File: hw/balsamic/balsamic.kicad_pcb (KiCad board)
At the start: 2 copper layers, 3 parts, among them U1 ISP1807-LR-RS, U2 BMI160, U3 K210

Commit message: Add hardware files
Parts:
- added J1: Conn_01x24, Connector_FFC-FPC:Hirose_FH12-24S-0.5SH_1x24-1MP_P0.50mm_Horizontal, F.Cu at (195.0, 35.1)
- added J2: USB_C_Receptacle_USB2.0, Connector_USB:USB_C_Receptacle_XKB_U262-16XN-4BVC11, F.Cu at (167.7, 38.7)
- added U4: CH552T, Package_SO:TSSOP-20_4.4x6.5mm_P0.65mm, F.Cu at (185.6, 31.8)
- added U5: GD25LQ, footprints:SOIC127P790X216-8N, F.Cu at (170.2, 25.7)
- moved U3 28.5 mm to (176.8, 39.9)
- moved U2 18.0 mm to (179.0, 33.9)
- moved U1 12.1 mm to (185.6, 39.9)

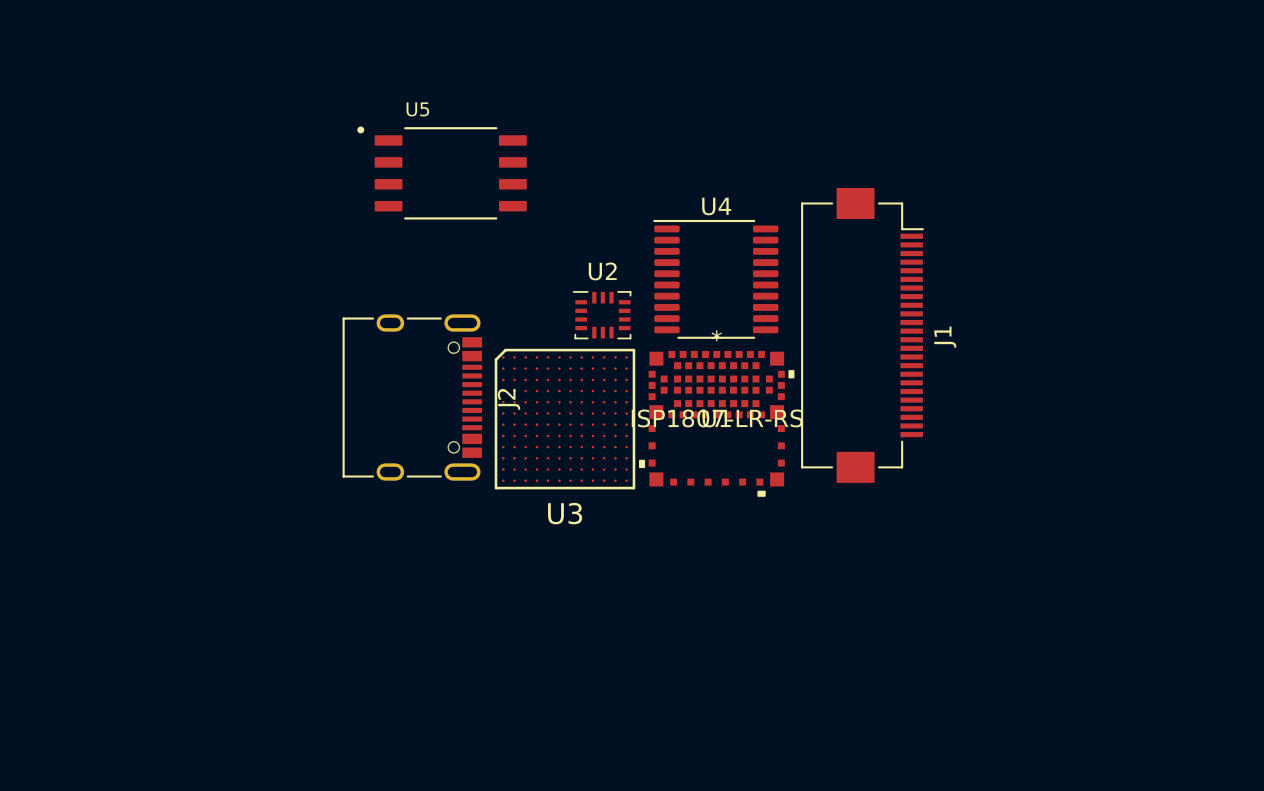
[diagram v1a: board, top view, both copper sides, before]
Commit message: PCB Schematic Layout
Finished schematic layout for MAX77658, power input to kendryte and some
of the signals for the kendryte IO.

I am beginning the layout for the ISP.
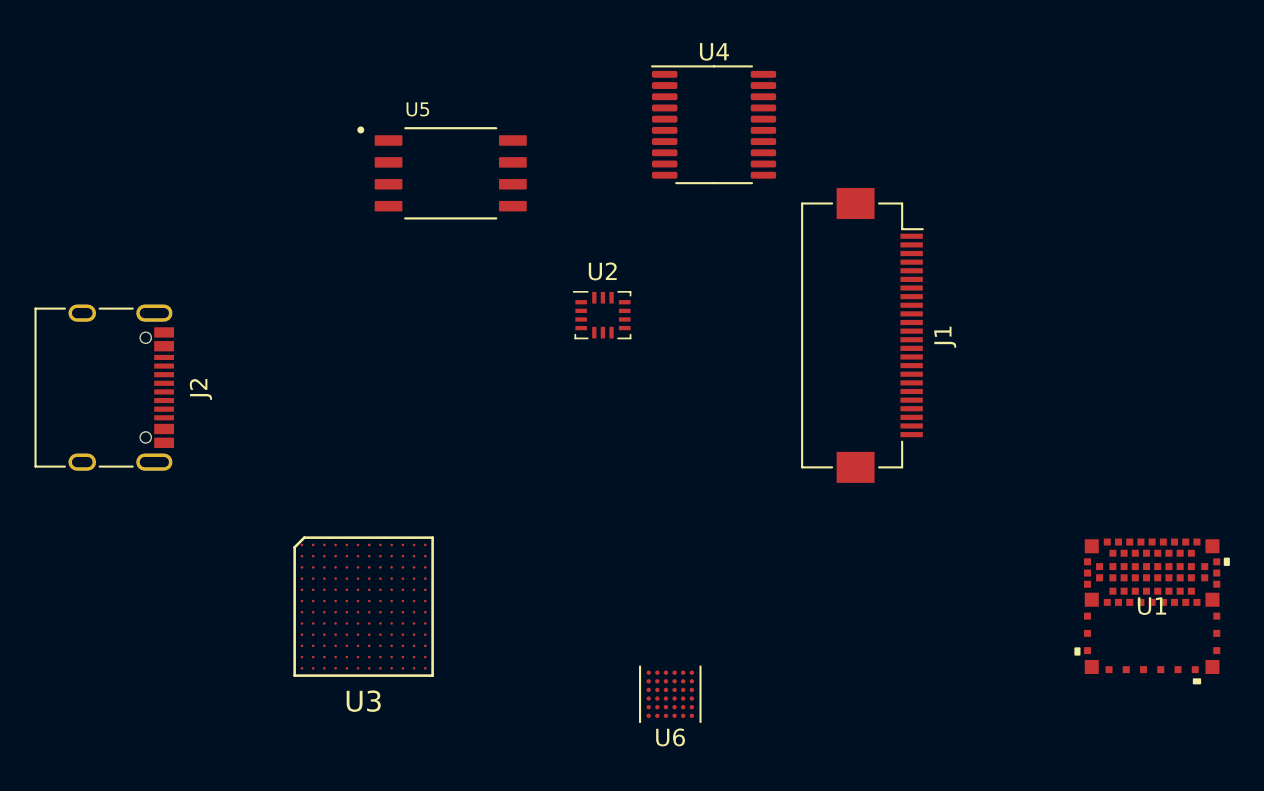
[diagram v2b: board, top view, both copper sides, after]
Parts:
- added U6: MAX77658AANX+, footprints:MAX77658AANX&plus_, F.Cu at (182.9, 55.9)
- moved U1 27.5 mm to (210.8, 50.8)
- moved J2 17.9 mm to (149.9, 38.1)
- moved U3 16.0 mm to (165.1, 50.8)
- moved U4 8.97 mm to (185.4, 22.9)
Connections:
- J1 pad 1: Net-(J1-Pad1) -> unconnected-(J1-Pad1)
- J1 pad 10: Net-(J1-Pad10) -> unconnected-(J1-Pad10)
- J1 pad 11: Net-(J1-Pad11) -> unconnected-(J1-Pad11)
- J1 pad 12: Net-(J1-Pad12) -> unconnected-(J1-Pad12)
- J1 pad 13: Net-(J1-Pad13) -> unconnected-(J1-Pad13)
- J1 pad 14: Net-(J1-Pad14) -> unconnected-(J1-Pad14)
- J1 pad 15: Net-(J1-Pad15) -> unconnected-(J1-Pad15)
- J1 pad 16: Net-(J1-Pad16) -> unconnected-(J1-Pad16)
- J1 pad 17: Net-(J1-Pad17) -> unconnected-(J1-Pad17)
- J1 pad 18: Net-(J1-Pad18) -> unconnected-(J1-Pad18)
- J1 pad 19: Net-(J1-Pad19) -> unconnected-(J1-Pad19)
- J1 pad 2: Net-(J1-Pad2) -> unconnected-(J1-Pad2)
- J1 pad 20: Net-(J1-Pad20) -> unconnected-(J1-Pad20)
- J1 pad 21: Net-(J1-Pad21) -> unconnected-(J1-Pad21)
- J1 pad 22: Net-(J1-Pad22) -> unconnected-(J1-Pad22)
- J1 pad 23: Net-(J1-Pad23) -> unconnected-(J1-Pad23)
- J1 pad 24: Net-(J1-Pad24) -> unconnected-(J1-Pad24)
- J1 pad 3: Net-(J1-Pad3) -> unconnected-(J1-Pad3)
- J1 pad 4: Net-(J1-Pad4) -> unconnected-(J1-Pad4)
- J1 pad 5: Net-(J1-Pad5) -> unconnected-(J1-Pad5)
- J1 pad 6: Net-(J1-Pad6) -> unconnected-(J1-Pad6)
- J1 pad 7: Net-(J1-Pad7) -> unconnected-(J1-Pad7)
- J1 pad 8: Net-(J1-Pad8) -> unconnected-(J1-Pad8)
- J1 pad 9: Net-(J1-Pad9) -> unconnected-(J1-Pad9)
- J2 pad A5: Net-(J2-PadA5) -> unconnected-(J2-PadA5)
- J2 pad A6: Net-(J2-PadA6) -> unconnected-(J2-PadA6)
- J2 pad A7: Net-(J2-PadA7) -> unconnected-(J2-PadA7)
- J2 pad A8: Net-(J2-PadA8) -> unconnected-(J2-PadA8)
- J2 pad B5: Net-(J2-PadB5) -> unconnected-(J2-PadB5)
- J2 pad B6: Net-(J2-PadB6) -> unconnected-(J2-PadB6)
- J2 pad B7: Net-(J2-PadB7) -> unconnected-(J2-PadB7)
- J2 pad B8: Net-(J2-PadB8) -> unconnected-(J2-PadB8)
- J2 pad S1: Net-(J2-PadS1) -> unconnected-(J2-PadS1)
- U1 pad 1: Net-(U1-Pad1) -> unconnected-(U1-Pad1)
- U1 pad 10: Net-(U1-Pad10) -> unconnected-(U1-Pad10)
- U1 pad 11: Net-(U1-Pad11) -> unconnected-(U1-Pad11)
- U1 pad 12: Net-(U1-Pad12) -> unconnected-(U1-Pad12)
- U1 pad 13: Net-(U1-Pad13) -> unconnected-(U1-Pad13)
- U1 pad 14: Net-(U1-Pad14) -> unconnected-(U1-Pad14)
- U1 pad 15: Net-(U1-Pad15) -> unconnected-(U1-Pad15)
- U1 pad 16: Net-(U1-Pad16) -> unconnected-(U1-Pad16)
- U1 pad 17: Net-(U1-Pad17) -> unconnected-(U1-Pad17)
- U1 pad 18: Net-(U1-Pad18) -> unconnected-(U1-Pad18)
- U1 pad 19: Net-(U1-Pad19) -> unconnected-(U1-Pad19)
- U1 pad 2: Net-(U1-Pad2) -> unconnected-(U1-Pad2)
- U1 pad 20: Net-(U1-Pad20) -> unconnected-(U1-Pad20)
- U1 pad 21: Net-(U1-Pad21) -> unconnected-(U1-Pad21)
- U1 pad 22: Net-(U1-Pad22) -> unconnected-(U1-Pad22)
- U1 pad 23: Net-(U1-Pad23) -> unconnected-(U1-Pad23)
- U1 pad 24: Net-(U1-Pad24) -> unconnected-(U1-Pad24)
- U1 pad 25: Net-(U1-Pad25) -> unconnected-(U1-Pad25)
- U1 pad 26: Net-(U1-Pad26) -> unconnected-(U1-Pad26)
- U1 pad 27: Net-(U1-Pad27) -> unconnected-(U1-Pad27)
- U1 pad 28: Net-(U1-Pad28) -> unconnected-(U1-Pad28)
- U1 pad 29: Net-(U1-Pad29) -> unconnected-(U1-Pad29)
- U1 pad 3: Net-(U1-Pad3) -> unconnected-(U1-Pad3)
- U1 pad 30: Net-(U1-Pad30) -> unconnected-(U1-Pad30)
- U1 pad 31: Net-(U1-Pad31) -> unconnected-(U1-Pad31)
- U1 pad 32: Net-(U1-Pad32) -> unconnected-(U1-Pad32)
- U1 pad 33: Net-(U1-Pad33) -> unconnected-(U1-Pad33)
- U1 pad 34: Net-(U1-Pad34) -> unconnected-(U1-Pad34)
- U1 pad 35: Net-(U1-Pad35) -> unconnected-(U1-Pad35)
- U1 pad 36: Net-(U1-Pad36) -> unconnected-(U1-Pad36)
- U1 pad 37: Net-(U1-Pad37) -> unconnected-(U1-Pad37)
- U1 pad 38: Net-(U1-Pad38) -> unconnected-(U1-Pad38)
- U1 pad 39: Net-(U1-Pad39) -> unconnected-(U1-Pad39)
- U1 pad 4: Net-(U1-Pad4) -> unconnected-(U1-Pad4)
- U1 pad 40: Net-(U1-Pad40) -> unconnected-(U1-Pad40)
- U1 pad 41: Net-(U1-Pad41) -> unconnected-(U1-Pad41)
- U1 pad 42: Net-(U1-Pad42) -> unconnected-(U1-Pad42)
- U1 pad 43: Net-(U1-Pad43) -> unconnected-(U1-Pad43)
- U1 pad 44: Net-(U1-Pad44) -> unconnected-(U1-Pad44)
- U1 pad 45: Net-(U1-Pad45) -> unconnected-(U1-Pad45)
- U1 pad 46: Net-(U1-Pad46) -> unconnected-(U1-Pad46)
- U1 pad 47: Net-(U1-Pad47) -> unconnected-(U1-Pad47)
- U1 pad 48: Net-(U1-Pad48) -> unconnected-(U1-Pad48)
- U1 pad 49: Net-(U1-Pad49) -> unconnected-(U1-Pad49)
- U1 pad 5: Net-(U1-Pad5) -> unconnected-(U1-Pad5)
- U1 pad 50: Net-(U1-Pad50) -> unconnected-(U1-Pad50)
- U1 pad 51: Net-(U1-Pad51) -> unconnected-(U1-Pad51)
- U1 pad 52: Net-(U1-Pad52) -> unconnected-(U1-Pad52)
- U1 pad 53: Net-(U1-Pad53) -> unconnected-(U1-Pad53)
- U1 pad 54: Net-(U1-Pad54) -> unconnected-(U1-Pad54)
- U1 pad 55: Net-(U1-Pad55) -> unconnected-(U1-Pad55)
- U1 pad 56: Net-(U1-Pad56) -> unconnected-(U1-Pad56)
- U1 pad 57: Net-(U1-Pad57) -> unconnected-(U1-Pad57)
- U1 pad 58: Net-(U1-Pad58) -> unconnected-(U1-Pad58)
- U1 pad 59: Net-(U1-Pad59) -> unconnected-(U1-Pad59)
- U1 pad 6: Net-(U1-Pad6) -> unconnected-(U1-Pad6)
- U1 pad 60: Net-(U1-Pad60) -> unconnected-(U1-Pad60)
- U1 pad 61: Net-(U1-Pad61) -> unconnected-(U1-Pad61)
- U1 pad 62: Net-(U1-Pad62) -> unconnected-(U1-Pad62)
- U1 pad 63: Net-(U1-Pad63) -> unconnected-(U1-Pad63)
- U1 pad 64: Net-(U1-Pad64) -> unconnected-(U1-Pad64)
- U1 pad 65: Net-(U1-Pad65) -> unconnected-(U1-Pad65)
- U1 pad 66: Net-(U1-Pad66) -> unconnected-(U1-Pad66)
- U1 pad 67: Net-(U1-Pad67) -> unconnected-(U1-Pad67)
- U1 pad 68: Net-(U1-Pad68) -> unconnected-(U1-Pad68)
- U1 pad 69: Net-(U1-Pad69) -> unconnected-(U1-Pad69)
- U1 pad 7: Net-(U1-Pad7) -> unconnected-(U1-Pad7)
- U1 pad 70: Net-(U1-Pad70) -> unconnected-(U1-Pad70)
- U1 pad 71: Net-(U1-Pad71) -> unconnected-(U1-Pad71)
- U1 pad 72: Net-(U1-Pad72) -> unconnected-(U1-Pad72)
- U1 pad 73: Net-(U1-Pad73) -> unconnected-(U1-Pad73)
- U1 pad 74: Net-(U1-Pad74) -> unconnected-(U1-Pad74)
- U1 pad 75: Net-(U1-Pad75) -> unconnected-(U1-Pad75)
- U1 pad 76: Net-(U1-Pad76) -> unconnected-(U1-Pad76)
- U1 pad 77: Net-(U1-Pad77) -> unconnected-(U1-Pad77)
- U1 pad 78: Net-(U1-Pad78) -> unconnected-(U1-Pad78)
- U1 pad 8: Net-(U1-Pad8) -> unconnected-(U1-Pad8)
- U1 pad 9: Net-(U1-Pad9) -> unconnected-(U1-Pad9)
- U2 pad 1: Net-(U2-Pad1) -> unconnected-(U2-Pad1)
- U2 pad 10: Net-(U2-Pad10) -> unconnected-(U2-Pad10)
- U2 pad 11: Net-(U2-Pad11) -> unconnected-(U2-Pad11)
- U2 pad 12: Net-(U2-Pad12) -> unconnected-(U2-Pad12)
- U2 pad 13: Net-(U2-Pad13) -> unconnected-(U2-Pad13)
- U2 pad 14: Net-(U2-Pad14) -> unconnected-(U2-Pad14)
- U2 pad 2: Net-(U2-Pad2) -> unconnected-(U2-Pad2)
- U2 pad 3: Net-(U2-Pad3) -> unconnected-(U2-Pad3)
- U2 pad 4: Net-(U2-Pad4) -> unconnected-(U2-Pad4)
- U2 pad 5: Net-(U2-Pad5) -> unconnected-(U2-Pad5)
- U2 pad 6: Net-(U2-Pad6) -> unconnected-(U2-Pad6)
- U2 pad 7: Net-(U2-Pad7) -> unconnected-(U2-Pad7)
- U2 pad 8: Net-(U2-Pad8) -> unconnected-(U2-Pad8)
- U2 pad 9: Net-(U2-Pad9) -> unconnected-(U2-Pad9)
- U3 pad A1: Net-(U3-PadA1) -> unconnected-(U3-PadA1)
- U3 pad A10: Net-(U3-PadA10) -> unconnected-(U3-PadA10)
- U3 pad A11: Net-(U3-PadA11) -> unconnected-(U3-PadA11)
- U3 pad A12: Net-(U3-PadA12) -> unconnected-(U3-PadA12)
- U3 pad A2: Net-(U3-PadA2) -> unconnected-(U3-PadA2)
- U3 pad A3: Net-(U3-PadA3) -> unconnected-(U3-PadA3)
- U3 pad A4: Net-(U3-PadA4) -> unconnected-(U3-PadA4)
- U3 pad A5: Net-(U3-PadA5) -> unconnected-(U3-PadA5)
- U3 pad A6: Net-(U3-PadA6) -> unconnected-(U3-PadA6)
- U3 pad A7: Net-(U3-PadA7) -> unconnected-(U3-PadA7)
- U3 pad A8: Net-(U3-PadA8) -> unconnected-(U3-PadA8)
- U3 pad A9: Net-(U3-PadA9) -> unconnected-(U3-PadA9)
- U3 pad B1: Net-(U3-PadB1) -> unconnected-(U3-PadB1)
- U3 pad B10: Net-(U3-PadB10) -> unconnected-(U3-PadB10)
- U3 pad B11: Net-(U3-PadB11) -> unconnected-(U3-PadB11)
- U3 pad B12: Net-(U3-PadB12) -> unconnected-(U3-PadB12)
- U3 pad B2: Net-(U3-PadB2) -> unconnected-(U3-PadB2)
- U3 pad B3: Net-(U3-PadB3) -> unconnected-(U3-PadB3)
- U3 pad B4: Net-(U3-PadB4) -> unconnected-(U3-PadB4)
- U3 pad B5: Net-(U3-PadB5) -> unconnected-(U3-PadB5)
- U3 pad B6: Net-(U3-PadB6) -> unconnected-(U3-PadB6)
- U3 pad B7: Net-(U3-PadB7) -> unconnected-(U3-PadB7)
- U3 pad B8: Net-(U3-PadB8) -> unconnected-(U3-PadB8)
- U3 pad B9: Net-(U3-PadB9) -> unconnected-(U3-PadB9)
- U3 pad C1: Net-(U3-PadC1) -> unconnected-(U3-PadC1)
- U3 pad C10: Net-(U3-PadC10) -> unconnected-(U3-PadC10)
- U3 pad C11: Net-(U3-PadC11) -> unconnected-(U3-PadC11)
- U3 pad C12: Net-(U3-PadC12) -> unconnected-(U3-PadC12)
- U3 pad C2: Net-(U3-PadC2) -> unconnected-(U3-PadC2)
- U3 pad C3: Net-(U3-PadC3) -> unconnected-(U3-PadC3)
- U3 pad C4: Net-(U3-PadC4) -> unconnected-(U3-PadC4)
- U3 pad C5: Net-(U3-PadC5) -> unconnected-(U3-PadC5)
- U3 pad C6: Net-(U3-PadC6) -> unconnected-(U3-PadC6)
- U3 pad C7: Net-(U3-PadC7) -> unconnected-(U3-PadC7)
- U3 pad C8: Net-(U3-PadC8) -> unconnected-(U3-PadC8)
- U3 pad C9: Net-(U3-PadC9) -> unconnected-(U3-PadC9)
- U3 pad D1: Net-(U3-PadD1) -> unconnected-(U3-PadD1)
- U3 pad D10: Net-(U3-PadD10) -> unconnected-(U3-PadD10)
- U3 pad D11: Net-(U3-PadD11) -> unconnected-(U3-PadD11)
- U3 pad D12: Net-(U3-PadD12) -> unconnected-(U3-PadD12)
- U3 pad D2: Net-(U3-PadD2) -> unconnected-(U3-PadD2)
- U3 pad D3: Net-(U3-PadD3) -> unconnected-(U3-PadD3)
- U3 pad D4: Net-(U3-PadD4) -> unconnected-(U3-PadD4)
- U3 pad D5: Net-(U3-PadD5) -> unconnected-(U3-PadD5)
- U3 pad D6: Net-(U3-PadD6) -> unconnected-(U3-PadD6)
- U3 pad D7: Net-(U3-PadD7) -> unconnected-(U3-PadD7)
- U3 pad D8: Net-(U3-PadD8) -> unconnected-(U3-PadD8)
- U3 pad D9: Net-(U3-PadD9) -> unconnected-(U3-PadD9)
- U3 pad E1: Net-(U3-PadE1) -> unconnected-(U3-PadE1)
- U3 pad E10: Net-(U3-PadE10) -> unconnected-(U3-PadE10)
- U3 pad E11: Net-(U3-PadE11) -> unconnected-(U3-PadE11)
- U3 pad E12: Net-(U3-PadE12) -> unconnected-(U3-PadE12)
- U3 pad E2: Net-(U3-PadE2) -> unconnected-(U3-PadE2)
- U3 pad E3: Net-(U3-PadE3) -> unconnected-(U3-PadE3)
- U3 pad E4: Net-(U3-PadE4) -> unconnected-(U3-PadE4)
- U3 pad E5: Net-(U3-PadE5) -> unconnected-(U3-PadE5)
- U3 pad E6: Net-(U3-PadE6) -> unconnected-(U3-PadE6)
- U3 pad E7: Net-(U3-PadE7) -> unconnected-(U3-PadE7)
- U3 pad E8: Net-(U3-PadE8) -> unconnected-(U3-PadE8)
- U3 pad E9: Net-(U3-PadE9) -> unconnected-(U3-PadE9)
- U3 pad F1: Net-(U3-PadF1) -> unconnected-(U3-PadF1)
- U3 pad F10: Net-(U3-PadF10) -> unconnected-(U3-PadF10)
- U3 pad F11: Net-(U3-PadF11) -> unconnected-(U3-PadF11)
- U3 pad F12: Net-(U3-PadF12) -> unconnected-(U3-PadF12)
- U3 pad F2: Net-(U3-PadF2) -> unconnected-(U3-PadF2)
- U3 pad F3: Net-(U3-PadF3) -> unconnected-(U3-PadF3)
- U3 pad F4: Net-(U3-PadF4) -> unconnected-(U3-PadF4)
- U3 pad F5: Net-(U3-PadF5) -> unconnected-(U3-PadF5)
- U3 pad F6: Net-(U3-PadF6) -> unconnected-(U3-PadF6)
- U3 pad F7: Net-(U3-PadF7) -> unconnected-(U3-PadF7)
- U3 pad F8: Net-(U3-PadF8) -> unconnected-(U3-PadF8)
- U3 pad F9: Net-(U3-PadF9) -> unconnected-(U3-PadF9)
- U3 pad G1: Net-(U3-PadG1) -> unconnected-(U3-PadG1)
- U3 pad G10: Net-(U3-PadG10) -> unconnected-(U3-PadG10)
- U3 pad G11: Net-(U3-PadG11) -> unconnected-(U3-PadG11)
- U3 pad G12: Net-(U3-PadG12) -> unconnected-(U3-PadG12)
- U3 pad G2: Net-(U3-PadG2) -> unconnected-(U3-PadG2)
- U3 pad G3: Net-(U3-PadG3) -> unconnected-(U3-PadG3)
- U3 pad G4: Net-(U3-PadG4) -> unconnected-(U3-PadG4)
- U3 pad G5: Net-(U3-PadG5) -> unconnected-(U3-PadG5)
- U3 pad G6: Net-(U3-PadG6) -> unconnected-(U3-PadG6)
- U3 pad G7: Net-(U3-PadG7) -> unconnected-(U3-PadG7)
- U3 pad G8: Net-(U3-PadG8) -> unconnected-(U3-PadG8)
- U3 pad G9: Net-(U3-PadG9) -> unconnected-(U3-PadG9)
- U3 pad H1: Net-(U3-PadH1) -> unconnected-(U3-PadH1)
- U3 pad H10: Net-(U3-PadH10) -> unconnected-(U3-PadH10)
- U3 pad H11: Net-(U3-PadH11) -> unconnected-(U3-PadH11)
- U3 pad H12: Net-(U3-PadH12) -> unconnected-(U3-PadH12)
- U3 pad H2: Net-(U3-PadH2) -> unconnected-(U3-PadH2)
- U3 pad H3: Net-(U3-PadH3) -> unconnected-(U3-PadH3)
- U3 pad H4: Net-(U3-PadH4) -> unconnected-(U3-PadH4)
- U3 pad H5: Net-(U3-PadH5) -> unconnected-(U3-PadH5)
- U3 pad H6: Net-(U3-PadH6) -> unconnected-(U3-PadH6)
- U3 pad H7: Net-(U3-PadH7) -> unconnected-(U3-PadH7)
- U3 pad H8: Net-(U3-PadH8) -> unconnected-(U3-PadH8)
- U3 pad H9: Net-(U3-PadH9) -> unconnected-(U3-PadH9)
- U3 pad J1: Net-(U3-PadJ1) -> unconnected-(U3-PadJ1)
- U3 pad J10: Net-(U3-PadJ10) -> unconnected-(U3-PadJ10)
- U3 pad J11: Net-(U3-PadJ11) -> unconnected-(U3-PadJ11)
- U3 pad J12: Net-(U3-PadJ12) -> unconnected-(U3-PadJ12)
- U3 pad J2: Net-(U3-PadJ2) -> unconnected-(U3-PadJ2)
- U3 pad J3: Net-(U3-PadJ3) -> unconnected-(U3-PadJ3)
- U3 pad J4: Net-(U3-PadJ4) -> unconnected-(U3-PadJ4)
- U3 pad J5: Net-(U3-PadJ5) -> unconnected-(U3-PadJ5)
- U3 pad J6: Net-(U3-PadJ6) -> unconnected-(U3-PadJ6)
- U3 pad J7: Net-(U3-PadJ7) -> unconnected-(U3-PadJ7)
- U3 pad J8: Net-(U3-PadJ8) -> unconnected-(U3-PadJ8)
- U3 pad J9: Net-(U3-PadJ9) -> unconnected-(U3-PadJ9)
- U3 pad K1: Net-(U3-PadK1) -> unconnected-(U3-PadK1)
- U3 pad K10: Net-(U3-PadK10) -> unconnected-(U3-PadK10)
- U3 pad K11: Net-(U3-PadK11) -> unconnected-(U3-PadK11)
- U3 pad K12: Net-(U3-PadK12) -> unconnected-(U3-PadK12)
- U3 pad K2: Net-(U3-PadK2) -> unconnected-(U3-PadK2)
- U3 pad K3: Net-(U3-PadK3) -> unconnected-(U3-PadK3)
- U3 pad K4: Net-(U3-PadK4) -> unconnected-(U3-PadK4)
- U3 pad K5: Net-(U3-PadK5) -> unconnected-(U3-PadK5)
- U3 pad K6: Net-(U3-PadK6) -> unconnected-(U3-PadK6)
- U3 pad K7: Net-(U3-PadK7) -> unconnected-(U3-PadK7)
- U3 pad K8: Net-(U3-PadK8) -> unconnected-(U3-PadK8)
- U3 pad K9: Net-(U3-PadK9) -> unconnected-(U3-PadK9)
- U3 pad L1: Net-(U3-PadL1) -> unconnected-(U3-PadL1)
- U3 pad L10: Net-(U3-PadL10) -> unconnected-(U3-PadL10)
- U3 pad L11: Net-(U3-PadL11) -> unconnected-(U3-PadL11)
- U3 pad L12: Net-(U3-PadL12) -> unconnected-(U3-PadL12)
- U3 pad L2: Net-(U3-PadL2) -> unconnected-(U3-PadL2)
- U3 pad L3: Net-(U3-PadL3) -> unconnected-(U3-PadL3)
- U3 pad L4: Net-(U3-PadL4) -> unconnected-(U3-PadL4)
- U3 pad L5: Net-(U3-PadL5) -> unconnected-(U3-PadL5)
- U3 pad L6: Net-(U3-PadL6) -> unconnected-(U3-PadL6)
- U3 pad L7: Net-(U3-PadL7) -> unconnected-(U3-PadL7)
- U3 pad L8: Net-(U3-PadL8) -> unconnected-(U3-PadL8)
- U3 pad L9: Net-(U3-PadL9) -> unconnected-(U3-PadL9)
- U3 pad M1: Net-(U3-PadM1) -> unconnected-(U3-PadM1)
- U3 pad M10: Net-(U3-PadM10) -> unconnected-(U3-PadM10)
- U3 pad M11: Net-(U3-PadM11) -> unconnected-(U3-PadM11)
- U3 pad M12: Net-(U3-PadM12) -> unconnected-(U3-PadM12)
- U3 pad M2: Net-(U3-PadM2) -> unconnected-(U3-PadM2)
- U3 pad M3: Net-(U3-PadM3) -> unconnected-(U3-PadM3)
- U3 pad M4: Net-(U3-PadM4) -> unconnected-(U3-PadM4)
- U3 pad M5: Net-(U3-PadM5) -> unconnected-(U3-PadM5)
- U3 pad M6: Net-(U3-PadM6) -> unconnected-(U3-PadM6)
- U3 pad M7: Net-(U3-PadM7) -> unconnected-(U3-PadM7)
- U3 pad M8: Net-(U3-PadM8) -> unconnected-(U3-PadM8)
- U3 pad M9: Net-(U3-PadM9) -> unconnected-(U3-PadM9)
- U4 pad 1: Net-(U4-Pad1) -> unconnected-(U4-Pad1)
- U4 pad 10: Net-(U4-Pad10) -> unconnected-(U4-Pad10)
- U4 pad 11: Net-(U4-Pad11) -> unconnected-(U4-Pad11)
- U4 pad 12: Net-(U4-Pad12) -> unconnected-(U4-Pad12)
- U4 pad 13: Net-(U4-Pad13) -> unconnected-(U4-Pad13)
- U4 pad 14: Net-(U4-Pad14) -> unconnected-(U4-Pad14)
- U4 pad 15: Net-(U4-Pad15) -> unconnected-(U4-Pad15)
- U4 pad 16: Net-(U4-Pad16) -> unconnected-(U4-Pad16)
- U4 pad 17: Net-(U4-Pad17) -> unconnected-(U4-Pad17)
- U4 pad 18: Net-(U4-Pad18) -> unconnected-(U4-Pad18)
- U4 pad 19: Net-(U4-Pad19) -> unconnected-(U4-Pad19)
- U4 pad 2: Net-(U4-Pad2) -> unconnected-(U4-Pad2)
- U4 pad 20: Net-(U4-Pad20) -> unconnected-(U4-Pad20)
- U4 pad 3: Net-(U4-Pad3) -> unconnected-(U4-Pad3)
- U4 pad 4: Net-(U4-Pad4) -> unconnected-(U4-Pad4)
- U4 pad 5: Net-(U4-Pad5) -> unconnected-(U4-Pad5)
- U4 pad 6: Net-(U4-Pad6) -> unconnected-(U4-Pad6)
- U4 pad 7: Net-(U4-Pad7) -> unconnected-(U4-Pad7)
- U4 pad 8: Net-(U4-Pad8) -> unconnected-(U4-Pad8)
- U4 pad 9: Net-(U4-Pad9) -> unconnected-(U4-Pad9)
- U5 pad 1: Net-(U5-Pad1) -> unconnected-(U5-Pad1)
- U5 pad 2: Net-(U5-Pad2) -> unconnected-(U5-Pad2)
- U5 pad 3: Net-(U5-Pad3) -> unconnected-(U5-Pad3)
- U5 pad 4: Net-(U5-Pad4) -> unconnected-(U5-Pad4)
- U5 pad 5: Net-(U5-Pad5) -> unconnected-(U5-Pad5)
- U5 pad 6: Net-(U5-Pad6) -> unconnected-(U5-Pad6)
- U5 pad 7: Net-(U5-Pad7) -> unconnected-(U5-Pad7)
- U5 pad 8: Net-(U5-Pad8) -> unconnected-(U5-Pad8)
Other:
- net class Default removed

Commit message: Began board Layout
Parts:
- added BT1: GREPOW_Battery, footprints:balsamic_grepow_battery, F.Cu at (52.5, 61.8)
- added C1: 4.7pF, Capacitor_SMD:C_0201_0603Metric, F.Cu at (78.3, 61.0)
- added C10: 22uF, Capacitor_SMD:C_0402_1005Metric, F.Cu at (79.5, 32.3)
- added C11: 4.7uF, Capacitor_SMD:C_0402_1005Metric, F.Cu at (54.0, 44.5)
- added C12: 10uF, Capacitor_SMD:C_0402_1005Metric, F.Cu at (54.0, 42.5)
- added C13: 100nF, Capacitor_SMD:C_0201_0603Metric, F.Cu at (79.7, 59.0)
- added C14: 1uF, Capacitor_SMD:C_0402_1005Metric, F.Cu at (73.3, 56.6)
- added C15: 10uF, Capacitor_SMD:C_0402_1005Metric, F.Cu at (54.0, 38.5)
- added C16: 22uF, Capacitor_SMD:C_0402_1005Metric, F.Cu at (85.4, 30.6)
- added C17: 10uF, Capacitor_SMD:C_0402_1005Metric, F.Cu at (54.0, 32.5)
- added C18: 10uF, Capacitor_SMD:C_0402_1005Metric, F.Cu at (79.9, 60.1)
- added C19: 10uF, Capacitor_SMD:C_0402_1005Metric, F.Cu at (54.0, 30.5)
- added C2: 4.7pF, Capacitor_SMD:C_0201_0603Metric, F.Cu at (74.5, 62.6)
- added C20: 10uF, Capacitor_SMD:C_0402_1005Metric, F.Cu at (66.8, 56.6)
- added C21: 10uF, Capacitor_SMD:C_0402_1005Metric, F.Cu at (68.1, 56.6)
- added C22: 10uF, Capacitor_SMD:C_0402_1005Metric, F.Cu at (54.0, 28.5)
- added C23: 1uF, Capacitor_SMD:C_0201_0603Metric, F.Cu at (78.0, 31.1)
- added C24: 100nF, Capacitor_SMD:C_0402_1005Metric, F.Cu at (68.1, 54.3)
- added C25: 100uF, Capacitor_SMD:C_0402_1005Metric, F.Cu at (54.0, 26.5)
- added C26: 100nF, Capacitor_SMD:C_0402_1005Metric, F.Cu at (69.4, 54.3)
- added C27: 100uF, Capacitor_SMD:C_0402_1005Metric, F.Cu at (54.0, 34.5)
- added C28: 1uF, Capacitor_SMD:C_0201_0603Metric, F.Cu at (78.0, 29.3)
- added C29: 100nF, Capacitor_SMD:C_0402_1005Metric, F.Cu at (69.4, 56.6)
- added C3: 100nF, Capacitor_SMD:C_0402_1005Metric, F.Cu at (178.7, 105.8)
- added C30: 100uF, Capacitor_SMD:C_0402_1005Metric, F.Cu at (54.0, 24.5)
- added C31: 10uF, Capacitor_SMD:C_0402_1005Metric, F.Cu at (76.3, 48.5)
- added C32: 100nF, Capacitor_SMD:C_0402_1005Metric, F.Cu at (72.0, 54.3)
- added C33: 10uF, Capacitor_SMD:C_0402_1005Metric, F.Cu at (83.8, 52.0)
- added C34: 10nF, Capacitor_SMD:C_0201_0603Metric, F.Cu at (80.6, 32.1)
- added C35: 100uF, Capacitor_SMD:C_0402_1005Metric, F.Cu at (54.0, 22.5)
- added C36: 22uF, Capacitor_SMD:C_0402_1005Metric, F.Cu at (83.7, 30.1)
- added C37: 10uF, Capacitor_SMD:C_0402_1005Metric, F.Cu at (76.3, 47.2)
- added C38: 10uF, Capacitor_SMD:C_0402_1005Metric, F.Cu at (85.1, 52.0)
- added C39: 0.47uF, Capacitor_SMD:C_0201_0603Metric, F.Cu at (83.8, 26.9)
- added C4: 22uF, Capacitor_SMD:C_0402_1005Metric, F.Cu at (85.4, 29.5)
- added C40: 100nF, Capacitor_SMD:C_0402_1005Metric, F.Cu at (70.7, 56.6)
- added C41: 100uF, Capacitor_SMD:C_0402_1005Metric, F.Cu at (54.0, 36.5)
- added C42: 100nF, Capacitor_SMD:C_0402_1005Metric, F.Cu at (73.3, 54.3)
- added C43: 100nF, Capacitor_SMD:C_0402_1005Metric, F.Cu at (70.7, 54.3)
- added C44: 100nF, Capacitor_SMD:C_0402_1005Metric, F.Cu at (72.0, 56.6)
- added C45: 100nF, Capacitor_SMD:C_0402_1005Metric, F.Cu at (112.0, 28.6)
- added C46: 100nF, Capacitor_SMD:C_0402_1005Metric, F.Cu at (112.0, 27.4)
- added C47: 22uF, Capacitor_SMD:C_0402_1005Metric, F.Cu at (51.9, 103.8)
- added C48: 10uF, Capacitor_SMD:C_0402_1005Metric, F.Cu at (58.8, 84.5)
- added C49: 10uF, Capacitor_SMD:C_0402_1005Metric, F.Cu at (49.0, 101.8)
- added C5: 4.7uF, Capacitor_SMD:C_0402_1005Metric, F.Cu at (54.0, 50.5)
- added C50: 100nf, Capacitor_SMD:C_0201_0603Metric, F.Cu at (59.9, 97.0)
- added C51: 10uF, Capacitor_SMD:C_0402_1005Metric, F.Cu at (175.1, 71.7)
- added C52: 1uF, Capacitor_SMD:C_0402_1005Metric, F.Cu at (167.4, 108.6)
- added C53: 1uF, Capacitor_SMD:C_0201_0603Metric, F.Cu at (78.0, 30.2)
- added C6: 4.7uF, Capacitor_SMD:C_0402_1005Metric, F.Cu at (54.0, 48.5)
- added C7: 4.7uF, Capacitor_SMD:C_0402_1005Metric, F.Cu at (77.8, 28.1)
- added C8: 4.7uF, Capacitor_SMD:C_0402_1005Metric, F.Cu at (54.0, 46.5)
- added C9: 4.7uF, Capacitor_SMD:C_0402_1005Metric, F.Cu at (54.0, 40.5)
- added D1: LED, LED_SMD:LED_0402_1005Metric, F.Cu at (100.4, 39.9)
- added D2: LED, LED_SMD:LED_0402_1005Metric, F.Cu at (100.4, 41.1)
- added FB1: FerriteBead_Small, Inductor_SMD:L_0201_0603Metric, F.Cu at (79.7, 61.3)
- added FB2: FerriteBead_Small, Inductor_SMD:L_0201_0603Metric, F.Cu at (78.3, 59.2)
- added L1: 1.5uH, Inductor_SMD:L_0805_2012Metric, F.Cu at (83.0, 32.2)
- added R1: 10k, Resistor_SMD:R_0201_0603Metric, F.Cu at (64.9, 49.1)
- added R10: 0, Resistor_SMD:R_0201_0603Metric, F.Cu at (81.6, 27.0)
- added R11: 4.7K, Resistor_SMD:R_0201_0603Metric, F.Cu at (78.1, 24.8)
- added R12: 4.7K, Resistor_SMD:R_0201_0603Metric, F.Cu at (78.1, 25.8)
- added R13: 0, Resistor_SMD:R_0201_0603Metric, F.Cu at (177.0, 103.5)
- added R14: NO_STUFF, Resistor_SMD:R_0201_0603Metric, F.Cu at (178.7, 103.8)
- added R15: 4.7K, Resistor_SMD:R_0201_0603Metric, F.Cu at (64.5, 90.0)
- added R16: 4.7K, Resistor_SMD:R_0201_0603Metric, F.Cu at (64.2, 88.1)
- added R17: 0, Resistor_SMD:R_0201_0603Metric, F.Cu at (50.3, 105.7)
- added R18: 0, Resistor_SMD:R_0201_0603Metric, F.Cu at (57.0, 101.3)
- added R19: 100k, Resistor_SMD:R_0201_0603Metric, F.Cu at (176.8, 73.7)
- added R2: 0, Resistor_SMD:R_0201_0603Metric, F.Cu at (73.9, 50.1)
- added R20: NO_STUFF, Resistor_SMD:R_0201_0603Metric, F.Cu at (115.5, 26.0)
- added R21: 0, Resistor_SMD:R_0402_1005Metric, F.Cu at (81.6, 76.3)
- added R22: 0, Resistor_SMD:R_0402_1005Metric, F.Cu at (75.8, 74.3)
- added R23: 0, Resistor_SMD:R_0402_1005Metric, F.Cu at (81.6, 72.3)
- added R24: 0, Resistor_SMD:R_0402_1005Metric, F.Cu at (75.8, 76.3)
- added R25: 0, Resistor_SMD:R_0402_1005Metric, F.Cu at (72.9, 76.3)
- added R26: 0, Resistor_SMD:R_0402_1005Metric, F.Cu at (81.6, 74.3)
- added R27: 0, Resistor_SMD:R_0402_1005Metric, F.Cu at (78.7, 76.3)
- added R28: 0, Resistor_SMD:R_0402_1005Metric, F.Cu at (72.9, 74.3)
- added R29: 0, Resistor_SMD:R_0402_1005Metric, F.Cu at (78.7, 74.3)
- added R3: 0, Resistor_SMD:R_0201_0603Metric, F.Cu at (57.0, 99.5)
- added R30: 0, Resistor_SMD:R_0402_1005Metric, F.Cu at (78.7, 72.3)
- added R31: 0, Resistor_SMD:R_0402_1005Metric, F.Cu at (72.9, 72.3)
- added R32: 0, Resistor_SMD:R_0402_1005Metric, F.Cu at (75.8, 72.3)
- added R33: 220, Resistor_SMD:R_0201_0603Metric, F.Cu at (98.2, 39.9)
- added R34: 220, Resistor_SMD:R_0201_0603Metric, F.Cu at (98.2, 41.1)
- added R35: 0, Resistor_SMD:R_0402_1005Metric, F.Cu at (49.8, 59.2)
- added R4: 5.1k, Resistor_SMD:R_0201_0603Metric, F.Cu at (117.4, 75.0)
- added R5: 5.1k, Resistor_SMD:R_0201_0603Metric, F.Cu at (117.3, 76.6)
- added R6: 1M, Resistor_SMD:R_0201_0603Metric, F.Cu at (67.5, 64.7)
- added R7: 1k, Resistor_SMD:R_0201_0603Metric, F.Cu at (117.3, 73.7)
- added R8: 2k, Resistor_SMD:R_0201_0603Metric, F.Cu at (117.3, 78.3)
- added R9: 100k, Resistor_SMD:R_0201_0603Metric, F.Cu at (85.3, 28.2)
- added SW1: SW_Push, Button_Switch_SMD:SW_SPST_B3U-1000P, F.Cu at (131.3, 92.7)
- added TP1: TestPoint, TestPoint:TestPoint_Pad_1.0x1.0mm, F.Cu at (233.3, 18.1)
- added TP10: TestPoint, TestPoint:TestPoint_Pad_1.0x1.0mm, F.Cu at (204.2, 18.1)
- added TP11: TestPoint, TestPoint:TestPoint_Pad_1.0x1.0mm, F.Cu at (180.0, 18.1)
- added TP12: TestPoint, TestPoint:TestPoint_Pad_1.0x1.0mm, F.Cu at (218.8, 18.1)
- added TP13: TestPoint, TestPoint:TestPoint_Pad_1.0x1.0mm, F.Cu at (228.4, 18.1)
- added TP14: TestPoint, TestPoint:TestPoint_Pad_1.0x1.0mm, F.Cu at (194.6, 18.1)
- added TP15: TestPoint, TestPoint:TestPoint_Pad_1.0x1.0mm, F.Cu at (213.9, 18.1)
- added TP16: TestPoint, TestPoint:TestPoint_Pad_1.0x1.0mm, F.Cu at (151.0, 18.1)
- added TP17: TestPoint, TestPoint:TestPoint_Pad_1.0x1.0mm, F.Cu at (170.4, 18.1)
- added TP18: TestPoint, TestPoint:TestPoint_Pad_1.0x1.0mm, F.Cu at (155.8, 18.1)
- added TP19: TestPoint, TestPoint:TestPoint_Pad_1.0x1.0mm, F.Cu at (160.7, 18.1)
- added TP2: TestPoint, TestPoint:TestPoint_Pad_1.0x1.0mm, F.Cu at (199.4, 18.1)
- added TP20: TestPoint, TestPoint:TestPoint_Pad_1.0x1.0mm, F.Cu at (175.2, 18.1)
- added TP3: TestPoint, TestPoint:TestPoint_Pad_1.0x1.0mm, F.Cu at (209.1, 18.1)
- added TP4: TestPoint, TestPoint:TestPoint_Pad_1.0x1.0mm, F.Cu at (189.7, 18.1)
- added TP5: TestPoint, TestPoint:TestPoint_Pad_1.0x1.0mm, F.Cu at (165.5, 18.1)
- added TP6: TestPoint, TestPoint:TestPoint_Pad_1.0x1.0mm, F.Cu at (223.6, 18.1)
- added TP7: TestPoint, TestPoint:TestPoint_Pad_1.0x1.0mm, F.Cu at (184.9, 18.1)
- added TP8: TestPoint, TestPoint:TestPoint_Pad_1.0x1.0mm, F.Cu at (243.0, 18.1)
- added TP9: TestPoint, TestPoint:TestPoint_Pad_1.0x1.0mm, F.Cu at (238.1, 18.1)
- added U7: SiP32431DR3, Package_TO_SOT_SMD:SOT-363_SC-70-6, F.Cu at (181.6, 105.6)
- added Y1: Crystal_GND24, Crystal:Crystal_SMD_3225-4Pin_3.2x2.5mm, F.Cu at (75.5, 60.1)
- J2: value USB_C_Receptacle_USB2.0 -> USB_C_Receptacle; footprint Connector_USB:USB_C_Receptacle_XKB_U262-16XN-4BVC11 -> Connector_USB:USB_C_Receptacle_Amphenol_12401610E4-2A
- U4: value CH552T -> MAX77658AANX+; footprint Package_SO:TSSOP-20_4.4x6.5mm_P0.65mm -> footprints:MAX77658AANX&plus_
- U6: value MAX77658AANX+ -> MAX811LEUS-T; footprint footprints:MAX77658AANX&plus_ -> Package_TO_SOT_SMD:SOT-143
- moved J1 127.3 mm to (79.9, 89.5), turned to 0 degrees
- moved U1 119.6 mm to (91.2, 53.4), turned to 90 degrees
- moved U4 104.6 mm to (81.0, 29.3)
- moved U3 86.4 mm to (78.7, 53.3)
- moved U5 81.5 mm to (173.1, 107.1)
- moved U2 66.6 mm to (113.0, 25.1)
- moved J2 66.2 mm to (106.8, 88.4), turned to 0 degrees
- moved U6 16.3 mm to (177.5, 71.3)
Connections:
- J1 pad 10: unconnected-(J1-Pad10) -> LDO_1
- J1 pad 11: unconnected-(J1-Pad11) -> LDO_1
- J1 pad 12: unconnected-(J1-Pad12) -> DVP_D7
- J1 pad 13: unconnected-(J1-Pad13) -> DVP_XCLK
- J1 pad 14: unconnected-(J1-Pad14) -> DVP_D6
- J1 pad 15: unconnected-(J1-Pad15) -> PGND
- J1 pad 16: unconnected-(J1-Pad16) -> DVP_D5
- J1 pad 17: unconnected-(J1-Pad17) -> DVP_PCLK
- J1 pad 18: unconnected-(J1-Pad18) -> DVP_D4
- J1 pad 19: unconnected-(J1-Pad19) -> DVP_D0
- J1 pad 2: unconnected-(J1-Pad2) -> GNDA
- J1 pad 20: unconnected-(J1-Pad20) -> DVP_D3
- J1 pad 21: unconnected-(J1-Pad21) -> DVP_D1
- J1 pad 22: unconnected-(J1-Pad22) -> DVP_D2
- J1 pad 23: unconnected-(J1-Pad23) -> Net-(J1-Pad23)
- J1 pad 24: unconnected-(J1-Pad24) -> Net-(J1-Pad24)
- J1 pad 3: unconnected-(J1-Pad3) -> DVP_SDA
- J1 pad 4: unconnected-(J1-Pad4) -> LDO_0
- J1 pad 5: unconnected-(J1-Pad5) -> DVP_SCL
- J1 pad 6: unconnected-(J1-Pad6) -> DVP_RST
- J1 pad 7: unconnected-(J1-Pad7) -> DVP_VSYNC
- J1 pad 8: unconnected-(J1-Pad8) -> DVP_PWDN
- J1 pad 9: unconnected-(J1-Pad9) -> DVP_HSYNC
- J2 pad A1: Net-(J2-PadA1) -> PGND
- J2 pad A12: Net-(J2-PadA1) -> PGND
- J2 pad A4: Net-(J2-PadA4) -> VBUS_USB
- J2 pad A5: unconnected-(J2-PadA5) -> Net-(J2-PadA5)
- J2 pad A6: unconnected-(J2-PadA6) -> Net-(J2-PadA6)
- J2 pad A7: unconnected-(J2-PadA7) -> Net-(J2-PadA7)
- J2 pad A8: unconnected-(J2-PadA8) -> nRF_UART_TX_DBUG
- J2 pad A9: Net-(J2-PadA4) -> VBUS_USB
- J2 pad B1: Net-(J2-PadA1) -> PGND
- J2 pad B12: Net-(J2-PadA1) -> PGND
- J2 pad B4: Net-(J2-PadA4) -> VBUS_USB
- J2 pad B5: unconnected-(J2-PadB5) -> Net-(J2-PadB5)
- J2 pad B6: unconnected-(J2-PadB6) -> Net-(J2-PadB6)
- J2 pad B7: unconnected-(J2-PadB7) -> Net-(J2-PadB7)
- J2 pad B8: unconnected-(J2-PadB8) -> nRF_UART_TX_DBUG
- J2 pad B9: Net-(J2-PadA4) -> VBUS_USB
- J2 pad S1: unconnected-(J2-PadS1) -> PGND
- U1 pad 1: unconnected-(U1-Pad1) -> PGND
- U1 pad 12: unconnected-(U1-Pad12) -> VBUS_USB
- U1 pad 13: unconnected-(U1-Pad13) -> nRF_RST
- U1 pad 14: unconnected-(U1-Pad14) -> PGND
- U1 pad 16: unconnected-(U1-Pad16) -> PGND
- U1 pad 18: unconnected-(U1-Pad18) -> PGND
- U1 pad 20: unconnected-(U1-Pad20) -> PGND
- U1 pad 21: unconnected-(U1-Pad21) -> PGND
- U1 pad 22: unconnected-(U1-Pad22) -> PGND
- U1 pad 23: unconnected-(U1-Pad23) -> PGND
- U1 pad 24: unconnected-(U1-Pad24) -> PGND
- U1 pad 25: unconnected-(U1-Pad25) -> PGND
- U1 pad 26: unconnected-(U1-Pad26) -> LDO_1
- U1 pad 28: unconnected-(U1-Pad28) -> USB_D-
- U1 pad 30: unconnected-(U1-Pad30) -> USB_D+
- U1 pad 31: unconnected-(U1-Pad31) -> PGND
- U1 pad 32: unconnected-(U1-Pad32) -> SPI_CLK
- U1 pad 33: unconnected-(U1-Pad33) -> SPI_CS_IMU
- U1 pad 34: unconnected-(U1-Pad34) -> SPI_MOSI
- U1 pad 35: unconnected-(U1-Pad35) -> SPI_MISO
- U1 pad 36: unconnected-(U1-Pad36) -> nRF_UART_TX
- U1 pad 37: unconnected-(U1-Pad37) -> nRF_UART_RX
- U1 pad 39: unconnected-(U1-Pad39) -> Button
- U1 pad 41: unconnected-(U1-Pad41) -> nRF_UART_RX_DBUG
- U1 pad 43: unconnected-(U1-Pad43) -> nRF_UART_TX_DBUG
- U1 pad 55: unconnected-(U1-Pad55) -> VDD_nRF
- U1 pad 56: unconnected-(U1-Pad56) -> PMU_SCL
- U1 pad 57: unconnected-(U1-Pad57) -> PMU_SDA
- U1 pad 58: unconnected-(U1-Pad58) -> nRF_LED2
- U1 pad 59: unconnected-(U1-Pad59) -> nRF_LED1
- U1 pad 60: unconnected-(U1-Pad60) -> INT_2_IMU
- U1 pad 61: unconnected-(U1-Pad61) -> INT_1_IMU
- U1 pad 62: unconnected-(U1-Pad62) -> NIRQ
- U1 pad 63: unconnected-(U1-Pad63) -> PMU_ALERT_PIN
- U1 pad 7: unconnected-(U1-Pad7) -> PGND
- U2 pad 1: unconnected-(U2-Pad1) -> SPI_MISO
- U2 pad 12: unconnected-(U2-Pad12) -> SPI_CS_IMU
- U2 pad 13: unconnected-(U2-Pad13) -> SPI_CLK
- U2 pad 14: unconnected-(U2-Pad14) -> SPI_MOSI
- U2 pad 4: unconnected-(U2-Pad4) -> INT_1_IMU
- U2 pad 5: unconnected-(U2-Pad5) -> VDD_nRF
- U2 pad 6: unconnected-(U2-Pad6) -> PGND
- U2 pad 7: unconnected-(U2-Pad7) -> PGND
- U2 pad 8: unconnected-(U2-Pad8) -> VDD_nRF
- U2 pad 9: unconnected-(U2-Pad9) -> INT_2_IMU
- U3 pad A1: unconnected-(U3-PadA1) -> Net-(R3-Pad1)
- U3 pad A2: unconnected-(U3-PadA2) -> Net-(R2-Pad2)
- U3 pad B12: unconnected-(U3-PadB12) -> BOOT_K210
- U3 pad C1: unconnected-(U3-PadC1) -> DVP_SCL
- U3 pad C10: unconnected-(U3-PadC10) -> PGND
- U3 pad C2: unconnected-(U3-PadC2) -> DVP_SDA
- U3 pad C3: unconnected-(U3-PadC3) -> PGND
- U3 pad C4: unconnected-(U3-PadC4) -> PGND
- U3 pad C5: unconnected-(U3-PadC5) -> SBB1_3.3V
- U3 pad C6: unconnected-(U3-PadC6) -> PGND
- U3 pad C7: unconnected-(U3-PadC7) -> SBB1_3.3V
- U3 pad C8: unconnected-(U3-PadC8) -> SBB1_3.3V
- U3 pad C9: unconnected-(U3-PadC9) -> PGND
- U3 pad D1: unconnected-(U3-PadD1) -> DVP_VSYNC
- U3 pad D10: unconnected-(U3-PadD10) -> SBB1_3.3V
- U3 pad D2: unconnected-(U3-PadD2) -> DVP_RST
- U3 pad D3: unconnected-(U3-PadD3) -> K210_1V8
- U3 pad D4: unconnected-(U3-PadD4) -> SBB2_0.9V
- U3 pad D5: unconnected-(U3-PadD5) -> PGND
- U3 pad D6: unconnected-(U3-PadD6) -> SBB2_0.9V
- U3 pad D7: unconnected-(U3-PadD7) -> PGND
- U3 pad D8: unconnected-(U3-PadD8) -> PGND
- U3 pad D9: unconnected-(U3-PadD9) -> SBB2_0.9V
- U3 pad E1: unconnected-(U3-PadE1) -> DVP_HSYNC
- U3 pad E10: unconnected-(U3-PadE10) -> PGND
- U3 pad E2: unconnected-(U3-PadE2) -> DVP_PWDN
- U3 pad E3: unconnected-(U3-PadE3) -> PGND
- U3 pad E4: unconnected-(U3-PadE4) -> PGND
- U3 pad E5: unconnected-(U3-PadE5) -> PGND
- U3 pad E6: unconnected-(U3-PadE6) -> PGND
- U3 pad E7: unconnected-(U3-PadE7) -> SBB2_0.9V
- U3 pad E8: unconnected-(U3-PadE8) -> PGND
- U3 pad E9: unconnected-(U3-PadE9) -> SBB2_0.9V
- U3 pad F1: unconnected-(U3-PadF1) -> DVP_PCLK
- U3 pad F10: unconnected-(U3-PadF10) -> PGND
- U3 pad F2: unconnected-(U3-PadF2) -> DVP_XCLK
- U3 pad F3: unconnected-(U3-PadF3) -> K210_1V8
- U3 pad F4: unconnected-(U3-PadF4) -> SBB2_0.9V
- U3 pad F5: unconnected-(U3-PadF5) -> PGND
- U3 pad F6: unconnected-(U3-PadF6) -> SBB2_0.9V
- U3 pad F7: unconnected-(U3-PadF7) -> PGND
- U3 pad F8: unconnected-(U3-PadF8) -> PGND
- U3 pad F9: unconnected-(U3-PadF9) -> PGND
- U3 pad G1: unconnected-(U3-PadG1) -> F_D1
- U3 pad G10: unconnected-(U3-PadG10) -> K210_1V8
- U3 pad G2: unconnected-(U3-PadG2) -> F_CS
- U3 pad G3: unconnected-(U3-PadG3) -> PGND
- U3 pad G4: unconnected-(U3-PadG4) -> PGND
- U3 pad G5: unconnected-(U3-PadG5) -> PGND
- U3 pad G6: unconnected-(U3-PadG6) -> PGND
- U3 pad G7: unconnected-(U3-PadG7) -> SBB2_0.9V
- U3 pad G8: unconnected-(U3-PadG8) -> PGND
- U3 pad G9: unconnected-(U3-PadG9) -> SBB2_0.9V
- U3 pad H1: unconnected-(U3-PadH1) -> F_D2
- U3 pad H10: unconnected-(U3-PadH10) -> SBB1_3.3V
- U3 pad H11: unconnected-(U3-PadH11) -> ISP_RX
- U3 pad H12: unconnected-(U3-PadH12) -> CH552_RX0
- U3 pad H2: unconnected-(U3-PadH2) -> PGND
- U3 pad H3: unconnected-(U3-PadH3) -> K210_1V8
- U3 pad H4: unconnected-(U3-PadH4) -> SBB2_0.9V
- U3 pad H5: unconnected-(U3-PadH5) -> PGND
- U3 pad H6: unconnected-(U3-PadH6) -> SBB2_0.9V
- U3 pad H7: unconnected-(U3-PadH7) -> PGND
- U3 pad H8: unconnected-(U3-PadH8) -> PGND
- U3 pad H9: unconnected-(U3-PadH9) -> PGND
- U3 pad J1: unconnected-(U3-PadJ1) -> F_D0
- U3 pad J10: unconnected-(U3-PadJ10) -> PGND
- U3 pad J11: unconnected-(U3-PadJ11) -> JTAG_TMS
- U3 pad J12: unconnected-(U3-PadJ12) -> JTAG_TDO
- U3 pad J2: unconnected-(U3-PadJ2) -> PGND
- U3 pad J3: unconnected-(U3-PadJ3) -> K210_1V8
- U3 pad J4: unconnected-(U3-PadJ4) -> PGND
- U3 pad J5: unconnected-(U3-PadJ5) -> SBB2_0.9V
- U3 pad J6: unconnected-(U3-PadJ6) -> PGND
- U3 pad J7: unconnected-(U3-PadJ7) -> SBB2_0.9V
- U3 pad J8: unconnected-(U3-PadJ8) -> PGND
- U3 pad J9: unconnected-(U3-PadJ9) -> SBB2_0.9V
- U3 pad K1: unconnected-(U3-PadK1) -> F_CLK
- U3 pad K10: unconnected-(U3-PadK10) -> PGND
- U3 pad K11: unconnected-(U3-PadK11) -> JTAG_TCK
- U3 pad K12: unconnected-(U3-PadK12) -> JTAG_TDI
- U3 pad K2: unconnected-(U3-PadK2) -> PGND
- U3 pad K3: unconnected-(U3-PadK3) -> PGND
- U3 pad K4: unconnected-(U3-PadK4) -> Net-(C13-Pad2)
- U3 pad K5: unconnected-(U3-PadK5) -> PGND
- U3 pad K6: unconnected-(U3-PadK6) -> K210_1V8
- U3 pad K7: unconnected-(U3-PadK7) -> PGND
- U3 pad K8: unconnected-(U3-PadK8) -> K210_1V8
- U3 pad K9: unconnected-(U3-PadK9) -> PGND
- U3 pad L1: unconnected-(U3-PadL1) -> F_D3
- U3 pad L2: unconnected-(U3-PadL2) -> PGND
- U3 pad L3: unconnected-(U3-PadL3) -> 26M_OUT_K210
- U3 pad L4: unconnected-(U3-PadL4) -> Net-(C13-Pad1)
- U3 pad M1: unconnected-(U3-PadM1) -> CH552_P1.0
- U3 pad M10: unconnected-(U3-PadM10) -> DVP_D2
- U3 pad M11: unconnected-(U3-PadM11) -> DVP_D1
- U3 pad M12: unconnected-(U3-PadM12) -> DVP_D0
- U3 pad M2: unconnected-(U3-PadM2) -> 26M_OUT_K210
- U3 pad M3: unconnected-(U3-PadM3) -> K210_X_OUT
- U3 pad M4: unconnected-(U3-PadM4) -> K210_X_IN
- U3 pad M5: unconnected-(U3-PadM5) -> DVP_D7
- U3 pad M6: unconnected-(U3-PadM6) -> DVP_D6
- U3 pad M7: unconnected-(U3-PadM7) -> DVP_D5
- U3 pad M8: unconnected-(U3-PadM8) -> DVP_D4
- U3 pad M9: unconnected-(U3-PadM9) -> DVP_D3
- U5 pad 1: unconnected-(U5-Pad1) -> F_CS
- U5 pad 2: unconnected-(U5-Pad2) -> F_D1
- U5 pad 3: unconnected-(U5-Pad3) -> F_D2
- U5 pad 4: unconnected-(U5-Pad4) -> PGND
- U5 pad 5: unconnected-(U5-Pad5) -> F_D0
- U5 pad 6: unconnected-(U5-Pad6) -> F_CLK
- U5 pad 7: unconnected-(U5-Pad7) -> F_D3
- U5 pad 8: unconnected-(U5-Pad8) -> K210_1V8
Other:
- rule pad_to_mask_clearance: 0.051 -> 0

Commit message: Board layout v.1
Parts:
- C1, C11, C12, C15, C17, C19, C2, C22, C25, C27, C3, C30, C35, C41, C47, C48, C49, C5, C50, C51, C52, C6, C8, C9, J1, R1, R13, R14, R15, R16, R17, R18, R19, R25, R26, R27, R28, R29, R35, R4, R5, U3, U5, U6, U7, Y1: moved to B.Cu
- moved R14 122.4 mm to (65.0, 58.4), turned to 0 degrees
- moved U7 122.1 mm to (68.4, 59.9)
- moved R13 121.9 mm to (65.1, 55.2)
- moved TP8 114.3 mm to (140.5, 68.7)
- moved R19 113.1 mm to (65.1, 56.1)
- moved C51 111.1 mm to (65.0, 57.1), turned to 0 degrees
- moved U6 110.8 mm to (67.7, 56.5)
- moved C3 109.3 mm to (82.4, 54.1), turned to 0 degrees
- moved TP9 108.9 mm to (140.5, 66.4)
- moved TP1 107.9 mm to (138.0, 68.7)
- moved U5 106.7 mm to (77.3, 60.1)
- moved TP13 105.9 mm to (135.4, 68.7)
- moved TP6 103.9 mm to (132.8, 68.7)
- moved TP12 101.9 mm to (130.3, 68.7)
- moved C52 100.4 mm to (82.4, 55.2), turned to 180 degrees
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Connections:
- C33 pad 1: LDO_1 -> K210_1V8
- C38 pad 1: LDO_1 -> K210_1V8
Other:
- board outline added: 24 x 39 mm
